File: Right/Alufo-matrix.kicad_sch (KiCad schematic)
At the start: 45 parts, among them K11 PG1350, K12 PG1350, K13 PG1350, K14 PG1350, K15 PG1350, K16 PG1350, K21 PG1350, K22 PG1350, K23 PG1350, K24 PG1350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

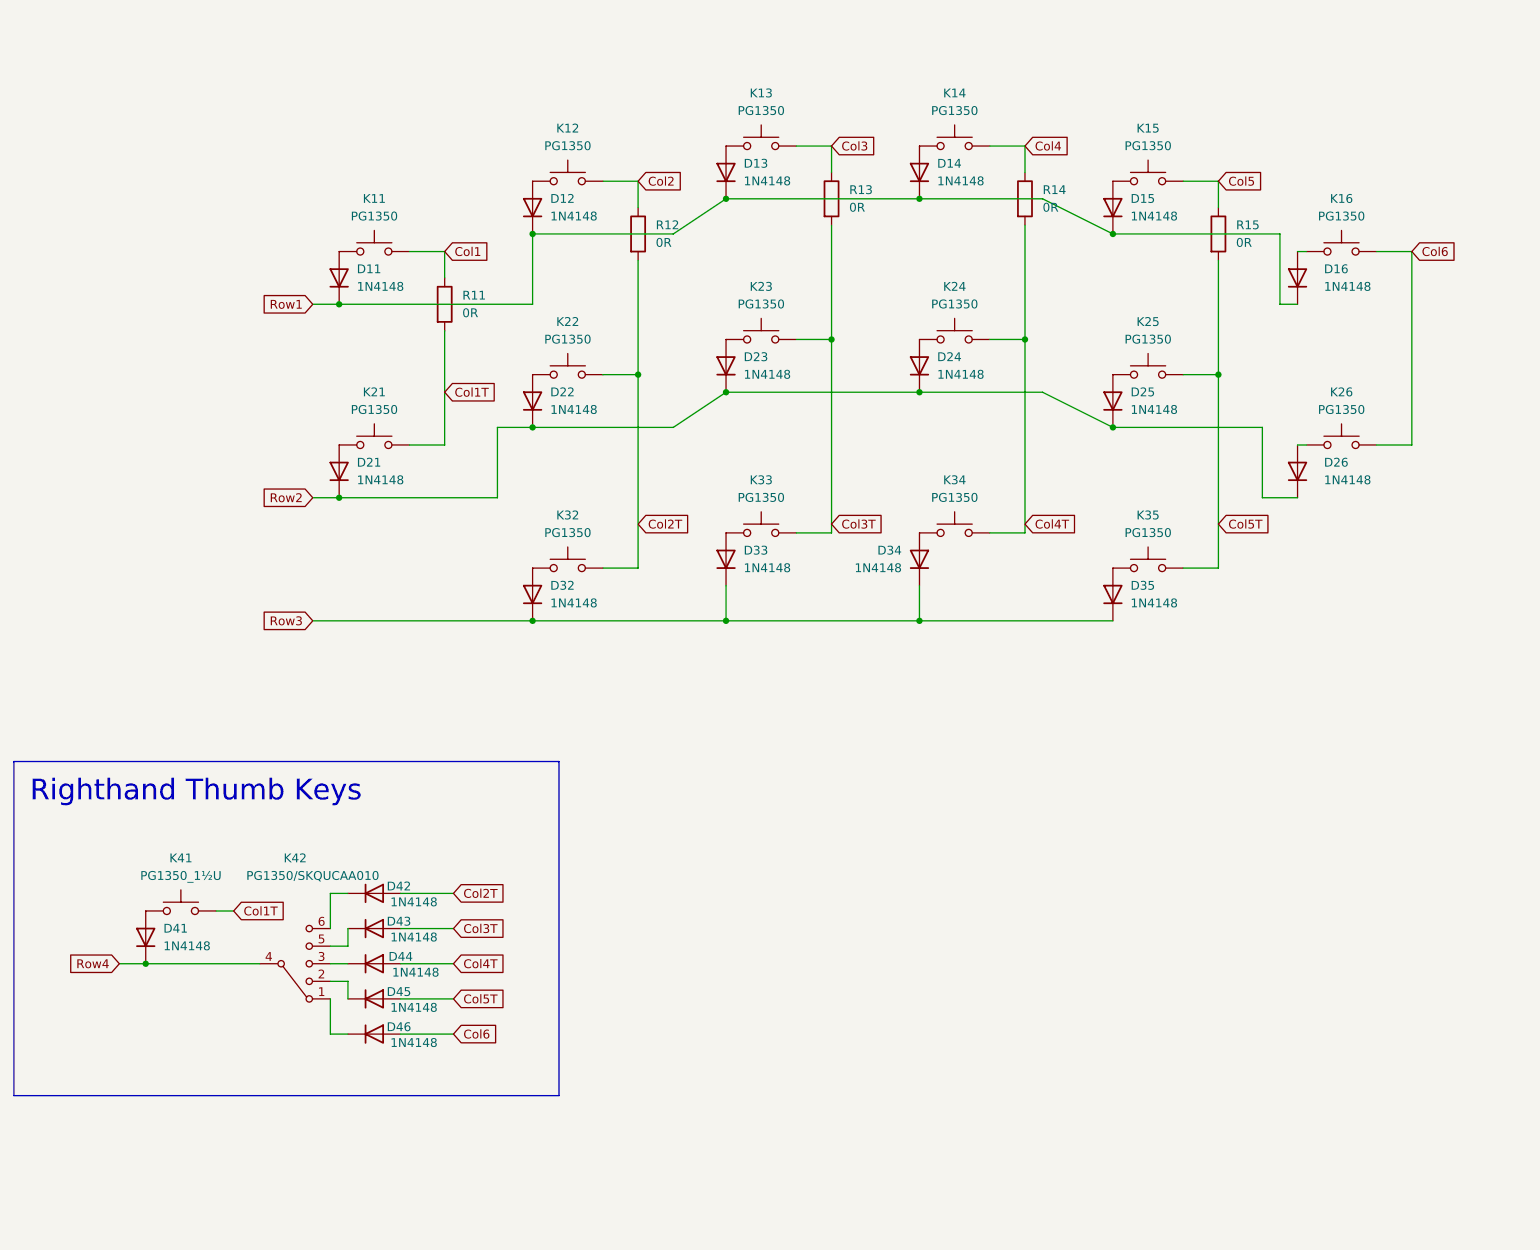
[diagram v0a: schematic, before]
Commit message: Add plate to righthand board
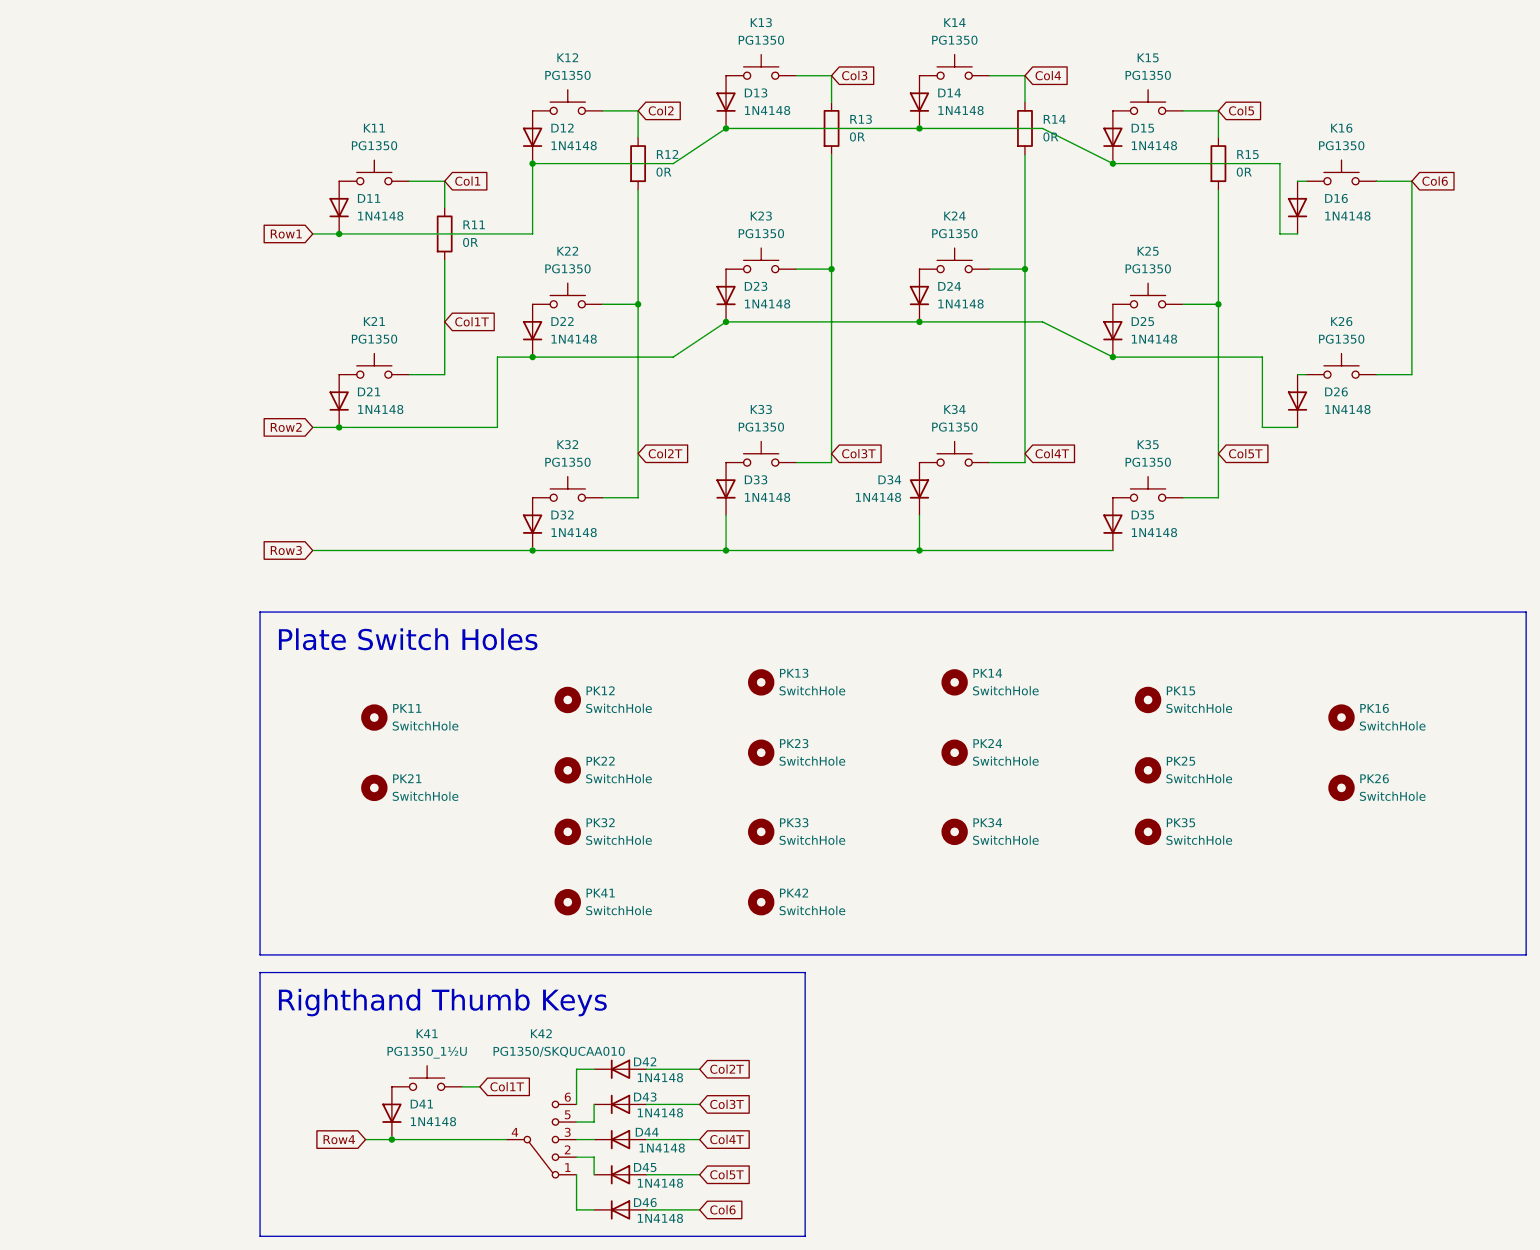
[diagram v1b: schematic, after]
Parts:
- added PK11, PK12, PK13, PK14, PK15, PK16, PK21, PK22, PK23, PK24, PK25, PK26, PK32, PK33, PK34, PK35, PK42: SwitchHole, Project Library:SW_choc_v1_Plate_CPG135001S30_1u, symbol Mechanical:MountingHole
- added PK41: SwitchHole, Project Library:SW_choc_v1_Plate_CPG135001S30_1.5u, symbol Mechanical:MountingHole
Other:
- moved on the sheet: D11, D12, D13, D14, D15, D16, D21, D22, D23, D24, D25, D26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
